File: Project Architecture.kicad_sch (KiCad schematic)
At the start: 0 parts

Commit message: First draft of the schematic
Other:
- sheet Section A - Title A renamed MCU
- sheet Section B - Title B renamed Peripherals
- added sheet External Connectors (EC.kicad_sch)
- added sheet HUB (HUB.kicad_sch)
- added sheet LoRa (LoRa.kicad_sch)
- added sheet Power Management (PM.kicad_sch)
- sheet MCU: file Section A - Title A.kicad_sch -> MCU.kicad_sch
- sheet MCU ports: added {ESP_USB}, {I2C}, {LTE}, {PWR_CTRL}, {RA_CTRL}, {RS485}, {SPI}; removed none
- sheet Peripherals: file Section B - TItle B.kicad_sch -> MCU_peripherals.kicad_sch
- sheet Peripherals ports: added {RS485}, {SPI}; removed none
- note removed: "Page 4"

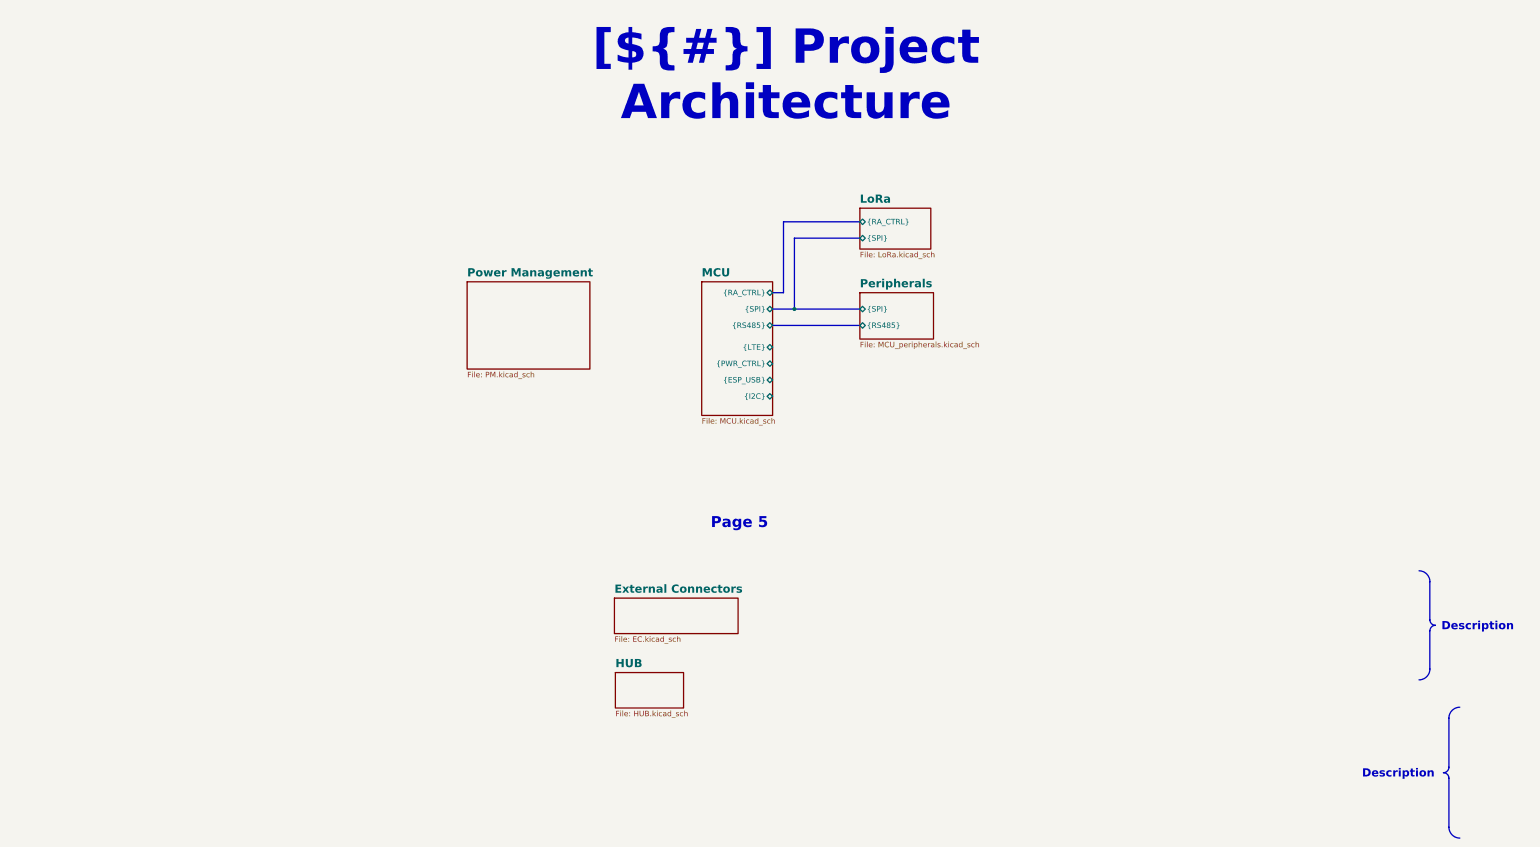
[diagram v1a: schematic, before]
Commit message: [Schematic][Added] Project Architecture, connectors
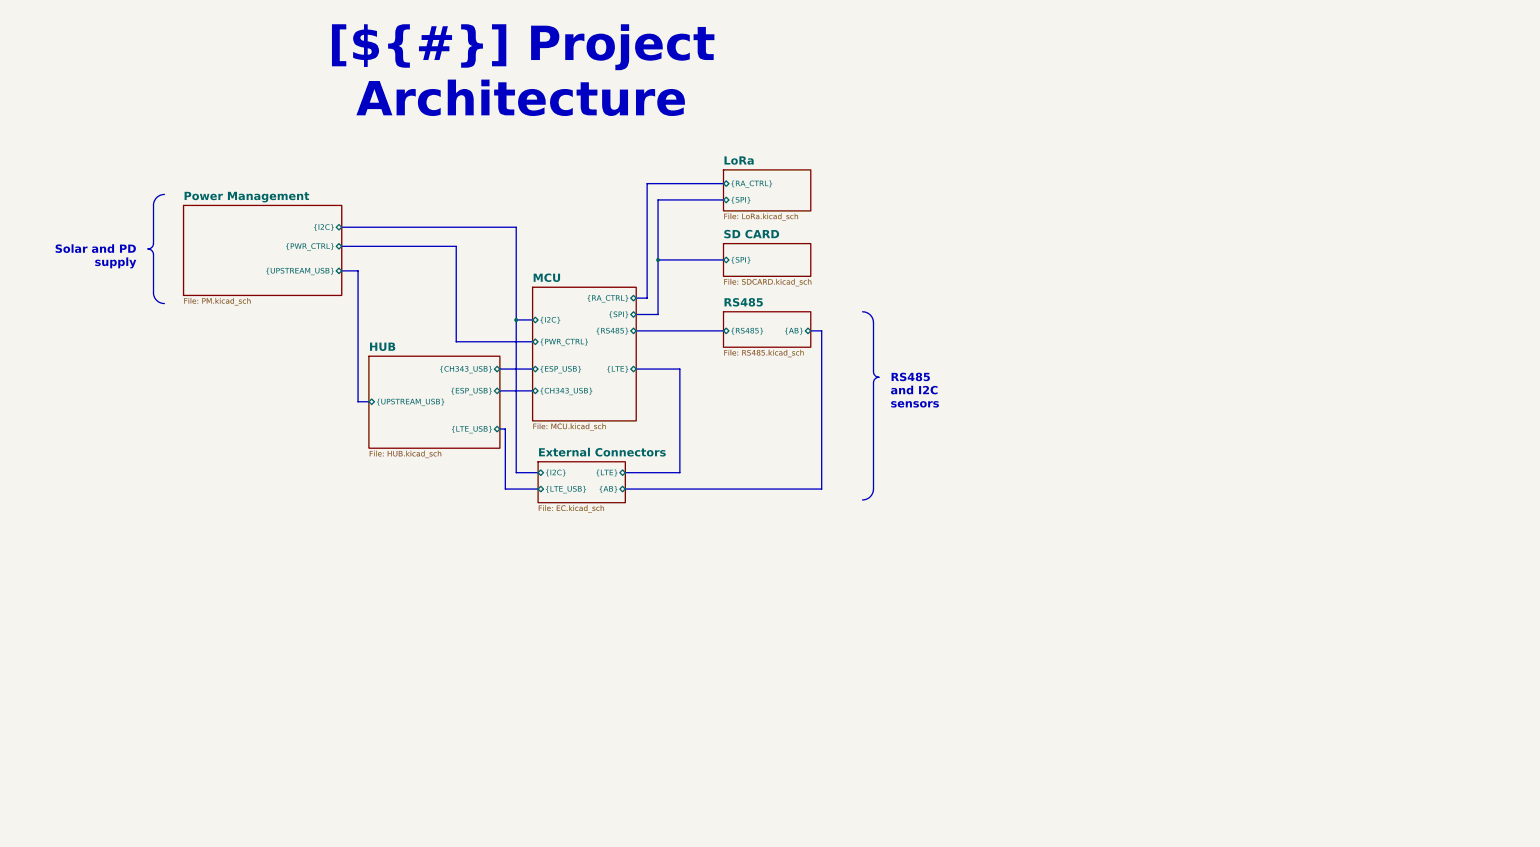
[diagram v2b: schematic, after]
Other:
- sheet Peripherals renamed SD CARD
- added sheet RS485 (RS485.kicad_sch)
- sheet External Connectors ports: added {AB}, {I2C}, {LTE_USB}, {LTE}; removed none
- sheet HUB ports: added {CH343_USB}, {ESP_USB}, {LTE_USB}, {UPSTREAM_USB}; removed none
- sheet MCU ports: added {CH343_USB}; removed none
- sheet Power Management ports: added {I2C}, {PWR_CTRL}, {UPSTREAM_USB}; removed none
- sheet SD CARD: file MCU_peripherals.kicad_sch -> SDCARD.kicad_sch
- sheet SD CARD ports: added none; removed {RS485}
- note removed: "Page 5"

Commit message: [PCB/SCH][Added] Preliminary version
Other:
- sheet External Connectors ports: added {GPIO}; removed none
- sheet MCU ports: added {GPIO}; removed none

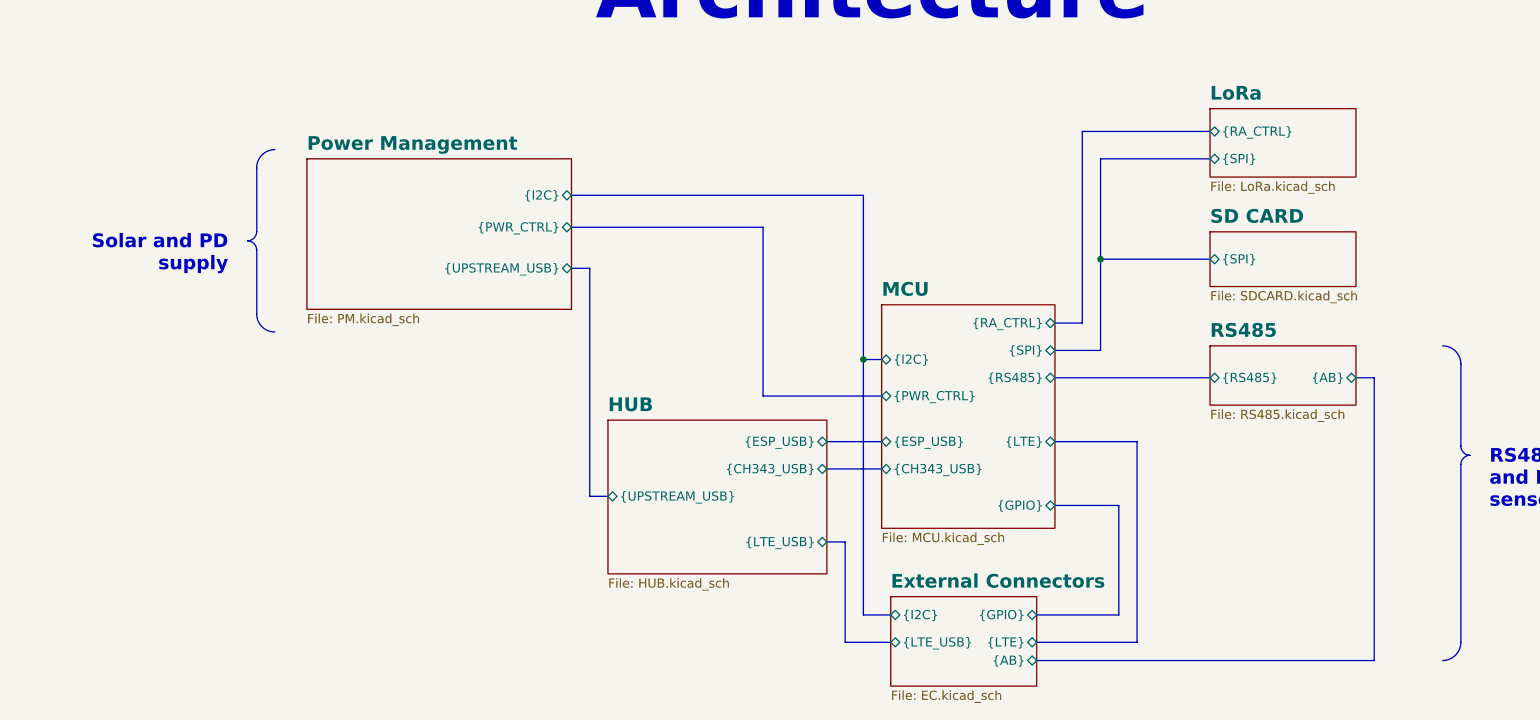
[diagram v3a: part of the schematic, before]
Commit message: [Schematic/PCB][Added] Connectors, layout, preliminar routing
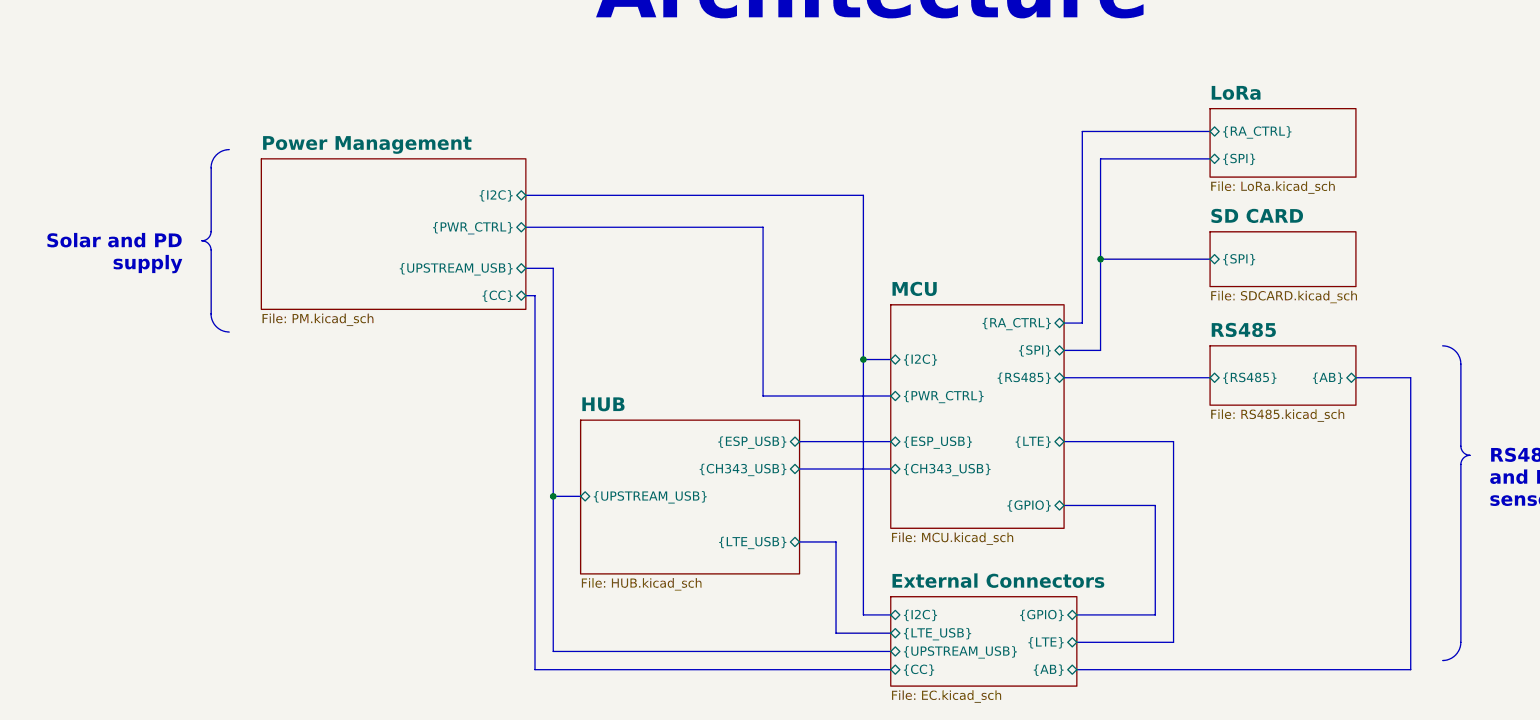
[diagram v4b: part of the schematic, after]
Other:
- sheet External Connectors ports: added {CC}, {UPSTREAM_USB}; removed none
- sheet Power Management ports: added {CC}; removed none

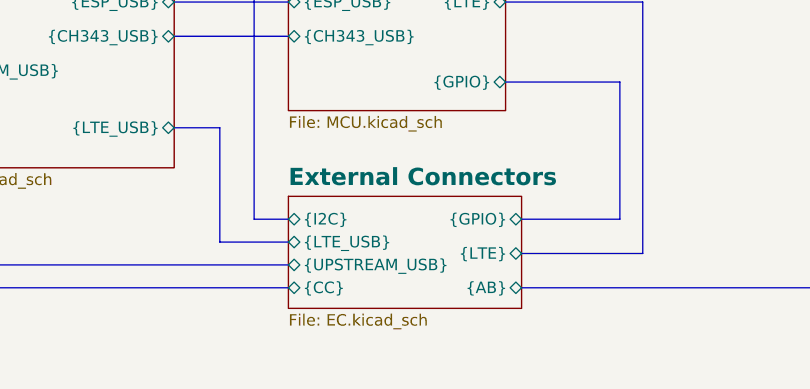
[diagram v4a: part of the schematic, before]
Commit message: [Schematic/PCB][Added] Routing almost finished
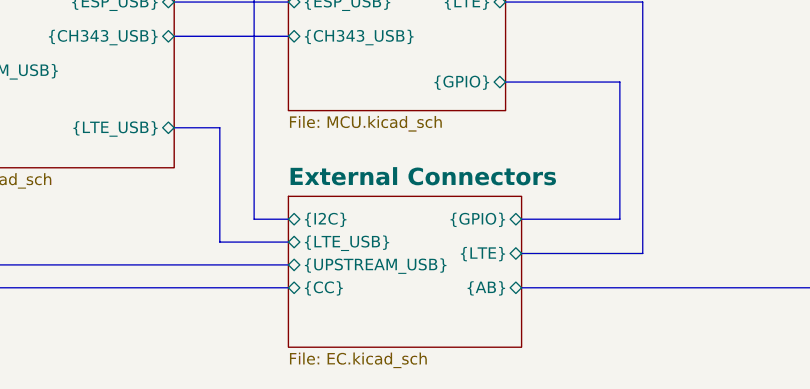
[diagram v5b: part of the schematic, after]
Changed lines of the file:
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@@
-	(bus
-		(pts
-			(xy 133.35 90.17) (xy 151.13 90.17)
-		)
-		(stroke
-			(width 0)
-			(type default)
-		)
-	)
 	(bus
 		(pts
@@
 		(pts
 			(xy 138.43 96.52) (xy 151.13 96.52)
+		)
+		(stroke
+			(width 0)
+			(type default)
+		)
+	)
+	(bus
+		(pts
+			(xy 133.35 90.17) (xy 151.13 90.17)
 		)
 		(stroke
@@
 	(sheet
 		(at 151.13 118.11)
-		(size 25.908 12.446)
+		(size 25.908 16.764)
 		(exclude_from_sim no)
 		(in_bom yes)
@@
 		)
 		(property "Sheetfile" "EC.kicad_sch"
-			(at 151.13 131.1406 0)
+			(at 151.13 135.4586 0)
 			(effects
 				(font
